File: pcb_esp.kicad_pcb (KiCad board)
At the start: 2 copper layers, 90 x 62 mm, 32 parts, among them J1 CONN_01X07, J2 CONN_01X03, J3 CONN_01X17, Q1 S8050, Q2 S8050, U1 LP38691, U2 ESP-12E, U3 ET024002DMU

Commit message: smd transistors + minor changes
transistors changed to smd
programming header changed to angled
minor routing and 3d model alignment changes
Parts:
- J1: footprint Pin_Headers:Pin_Header_Straight_1x07_Pitch2.54mm -> Pin_Headers:Pin_Header_Angled_1x07_Pitch2.54mm
- Q1, Q2: footprint TO_SOT_Packages_THT:TO-92_Molded_Narrow -> TO_SOT_Packages_SMD:SOT-23_Handsoldering; moved to B.Cu
- moved J1 15.2 mm to (127.0, 106.7), turned to 270 degrees
- moved R9 8.40 mm to (119.4, 97.2), turned to 180 degrees
- moved Q2 2.30 mm to (113.7, 98.4), turned to 180 degrees
- moved Q1 1.76 mm to (125.1, 98.4), turned to 0 degrees
- moved R7 0.35 mm to (119.4, 99.7), turned to 0 degrees
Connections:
- J1 pad 1: /dtr -> /rts
- J1 pad 2: /tx_gpio1 -> GND
- J1 pad 3: /rx_gpio3 -> /cts
- J1 pad 5: /cts -> /rx_gpio3
- J1 pad 6: GND -> /tx_gpio1
- J1 pad 7: /rts -> /dtr
- Q1 pad 1: /rts -> /dtr2
- Q1 pad 2: /dtr2 -> /rts
- Q2 pad 1: /dtr -> /rts2
- Q2 pad 2: /rts2 -> /dtr
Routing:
- net /rts2: track 17.5 -> 3.00 mm
- net /rts: track 12.5 -> 21.2 mm
- net /reset: track 148.5 -> 155.4 mm
- net /gpio0: track 127.7 -> 122.8 mm
- net /dtr: track 14.8 -> 11.7 mm
- net /dtr2: track 4.05 -> 3.00 mm

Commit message: routing
minor routing changes, moved a few vias, changed trace thickness a few places
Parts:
- moved R6 3.71 mm to (71.3, 65.3), turned to 270 degrees
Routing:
- net GND: track 102.0 -> 82.7 mm
- net /te_gpio2: track 63.7 -> 54.2 mm
- net Net-(R8-Pad2): track 8.47 -> 9.65 mm
- net /gpio4: track 85.3 -> 86.4 mm
- net +5V: track 93.6 -> 94.6 mm
- net /gpio0: track 122.8 -> 123.7 mm

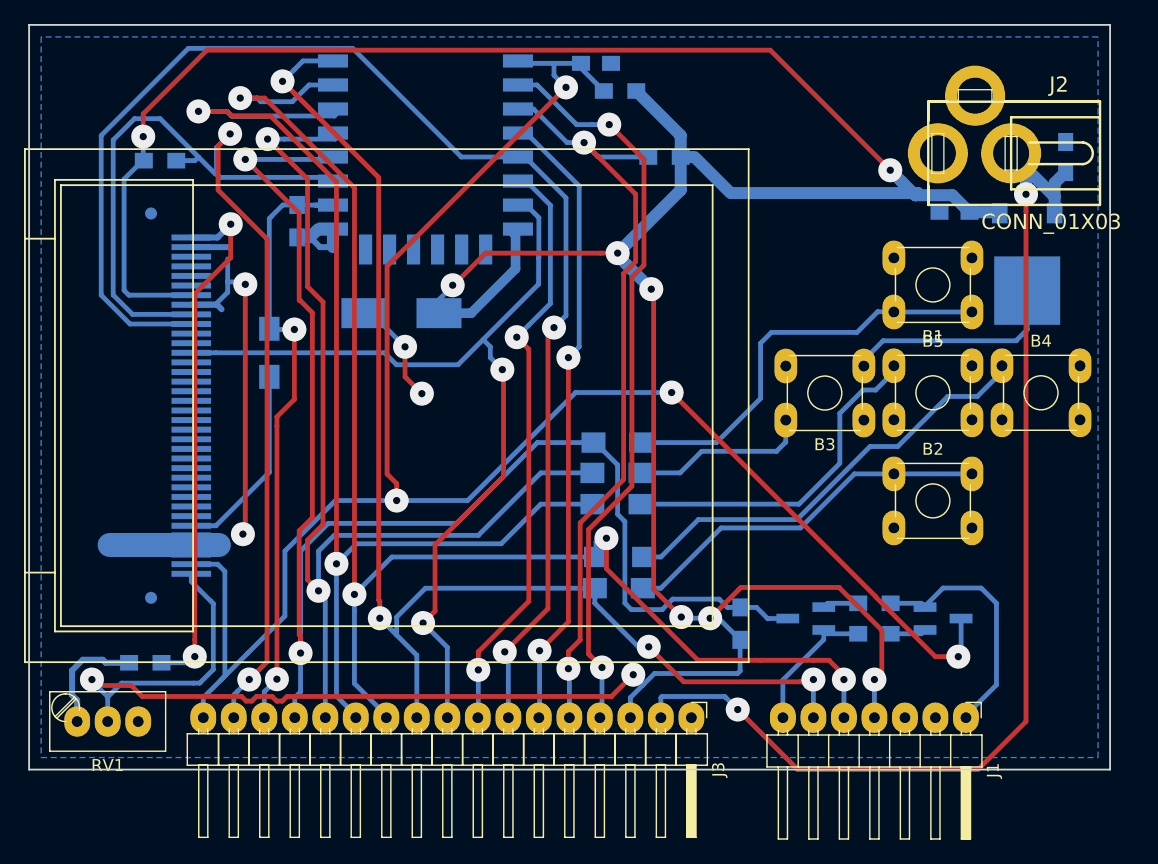
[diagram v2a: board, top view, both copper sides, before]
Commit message: Tweak vias a bit for easier soldering
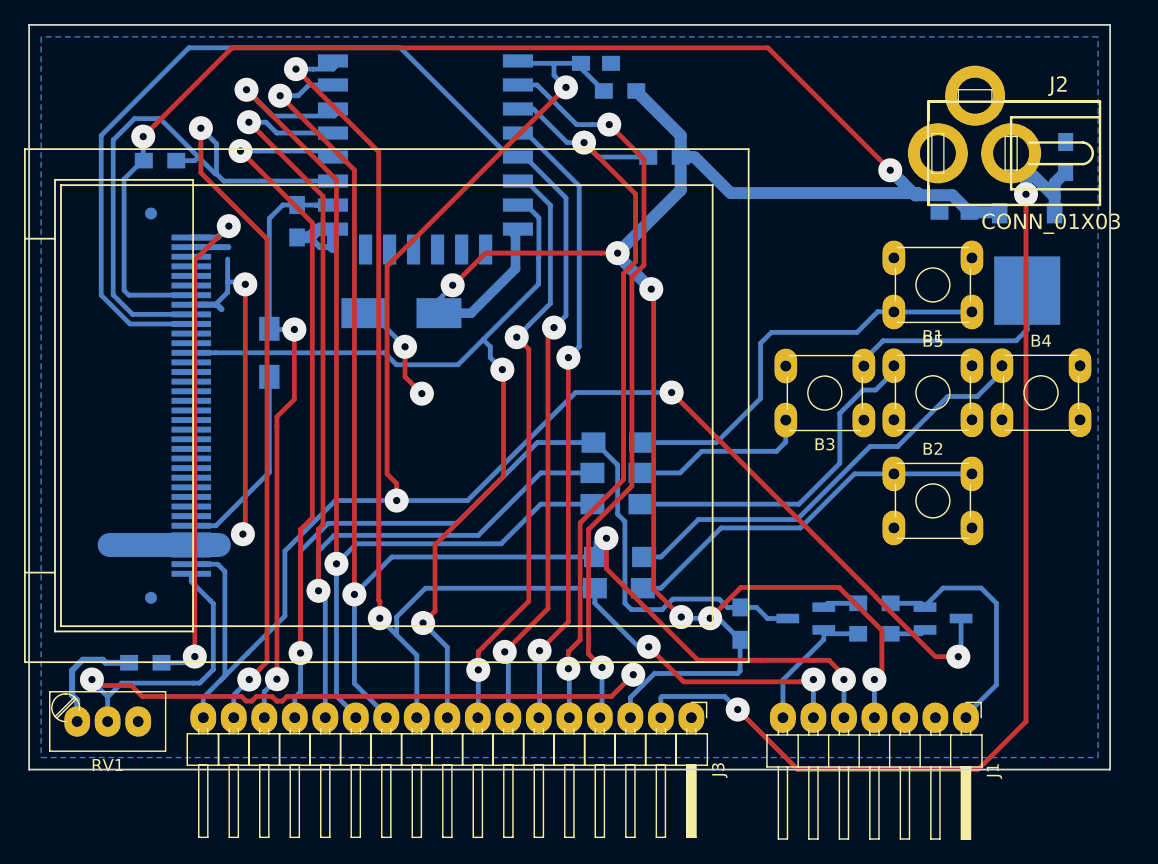
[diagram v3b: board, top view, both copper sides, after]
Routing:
- net /gpio5: track 94.9 -> 88.5 mm
- net /rx_gpio3: track 120.5 -> 114.5 mm
- net /gpio4: track 86.4 -> 89.4 mm
- net /gpio0: track 123.7 -> 125.0 mm
- net /cs_gpio15: track 99.6 -> 100.8 mm
- net /tx_gpio1: track 107.8 -> 106.8 mm
- net +3V3: track 314.5 -> 313.6 mm
